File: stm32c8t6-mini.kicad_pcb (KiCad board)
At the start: 2 copper layers, 48 x 32.5 mm, 40 parts, among them J1 Conn_01x07_Pin, J2 Conn_01x18_Pin, J3 Conn_01x18_Pin, P1 USB, SW1 Reset, SW2 BOOT0, U1 STM32F103C8Tx, U2 AMS1117, U3 USBLC6-2SC6, Y1 8MHz, Y2 32.768kHz

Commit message: Replace the USB-C socket type
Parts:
- removed P1: USB, WCH:TYPE-C-Receptacle-2.0
- added J4: USB_C_Receptacle_USB2.0_16P, Connector_USB:USB_C_Receptacle_HRO_TYPE-C-31-M-12, F.Cu at (110.2, 87.8)
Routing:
- net VBUS: track 32.4 -> 35.0 mm
- net Net-(J4-CC2): track 12.4 -> 11.2 mm
- net GND: track 43.8 -> 42.7 mm, vias 58 -> 60

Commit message: Remove and modify some words
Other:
- board text removed: "YONGCI"

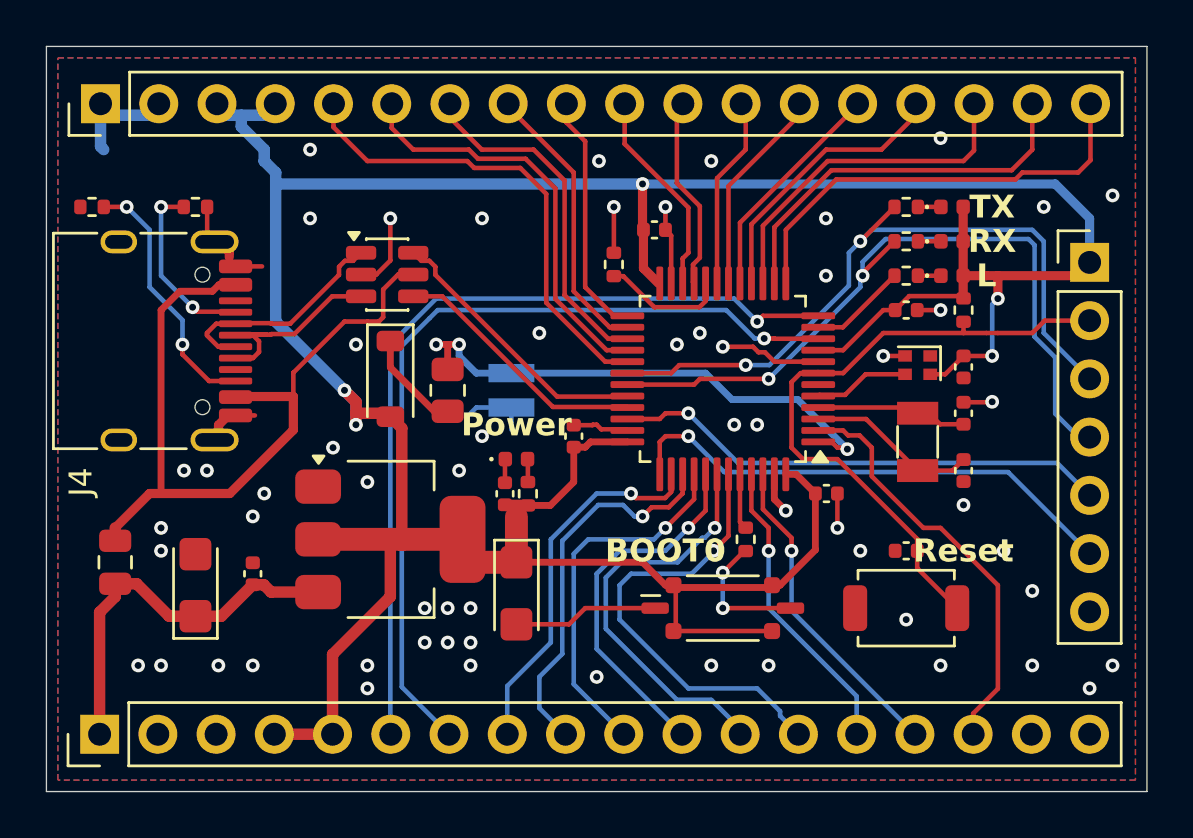
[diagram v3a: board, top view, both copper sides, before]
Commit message: Replace some components: 1. Replace the RTC super-capacitance to a 5.5mAh battery. 2. Replace the 1N5817-diode to 1SS367. 3. Replace the resister size from 0805 to 0603(0.1w~).
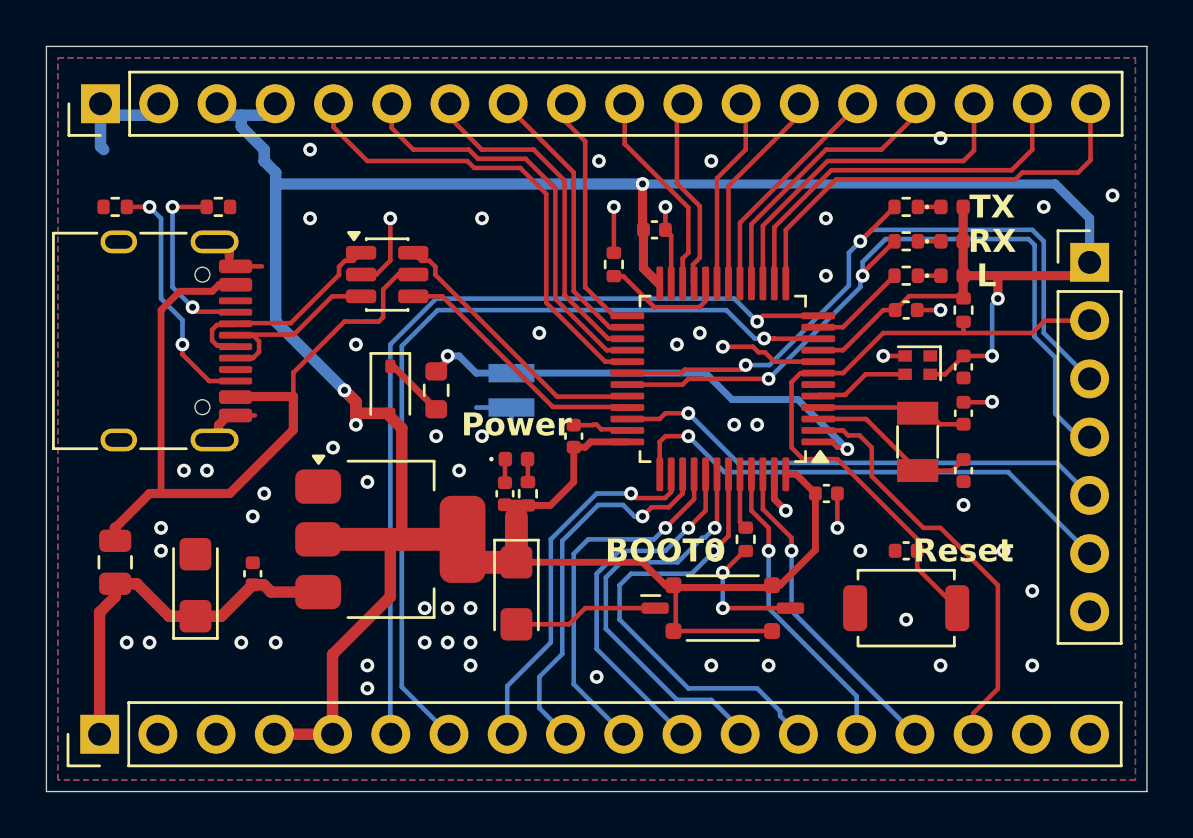
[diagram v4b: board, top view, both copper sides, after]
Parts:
- removed the C6 at (126.3, 90.0)
- added BT1: MS621FE,5.5mAh,3.3V, Battery:BatteryHolder_Seiko_MS621F, B.Cu at (126.3, 90.0)
- D1: value 1N5817 -> 1SS367; footprint Diode_SMD:D_SOD-123 -> Diode_SMD:D_SOD-323
- R10: value 620(1%0.8W) -> 620R(1%0.1W); footprint Resistor_SMD:R_0805_2012Metric -> Resistor_SMD:R_0603_1608Metric
- moved R2 1.01 mm to (109.0, 82.0)
- moved R1 1.00 mm to (113.5, 82.0)
- moved D1 0.50 mm to (121.0, 90.0)
- moved R10 0.50 mm to (123.0, 90.0)
- renumbered C11 to C10, C12 to C11, C13 to C12, C7 to C6, C8 to C7, C9 to C8, C10 to C9
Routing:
- net Net-(D1-K): track 4.99 -> 2.78 mm
- net /BAT+: track 23.6 -> 21.4 mm, vias 3 -> 2
- net GND: track 42.7 -> 41.2 mm, vias 60 -> 59
- net /USB_P: track 9.28 -> 8.68 mm
